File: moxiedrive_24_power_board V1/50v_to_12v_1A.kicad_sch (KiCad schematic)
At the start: 23 parts, among them J201 Conn_01x02, U201 SY8502

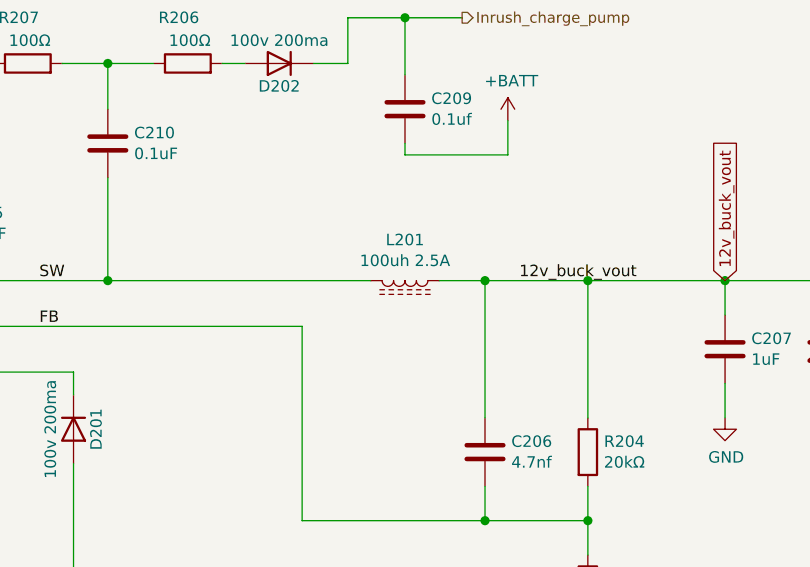
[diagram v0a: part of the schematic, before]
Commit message: fix misplaced component
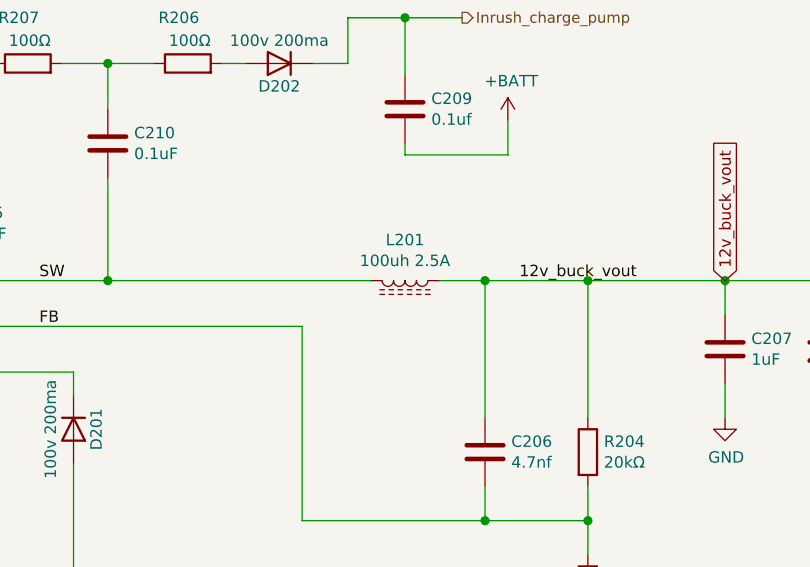
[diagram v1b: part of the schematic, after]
